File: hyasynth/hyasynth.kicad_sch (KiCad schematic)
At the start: 37 parts, among them J1 Conn_01x04_Male, J2 Conn_01x02_Male, J3 Conn_01x07_Male, J4 Conn_01x02_Male, J5 Conn_01x02_Male, SW1 Power Switch, SW10 G# Ab, SW11 A, SW12 A# Bb, SW13 B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

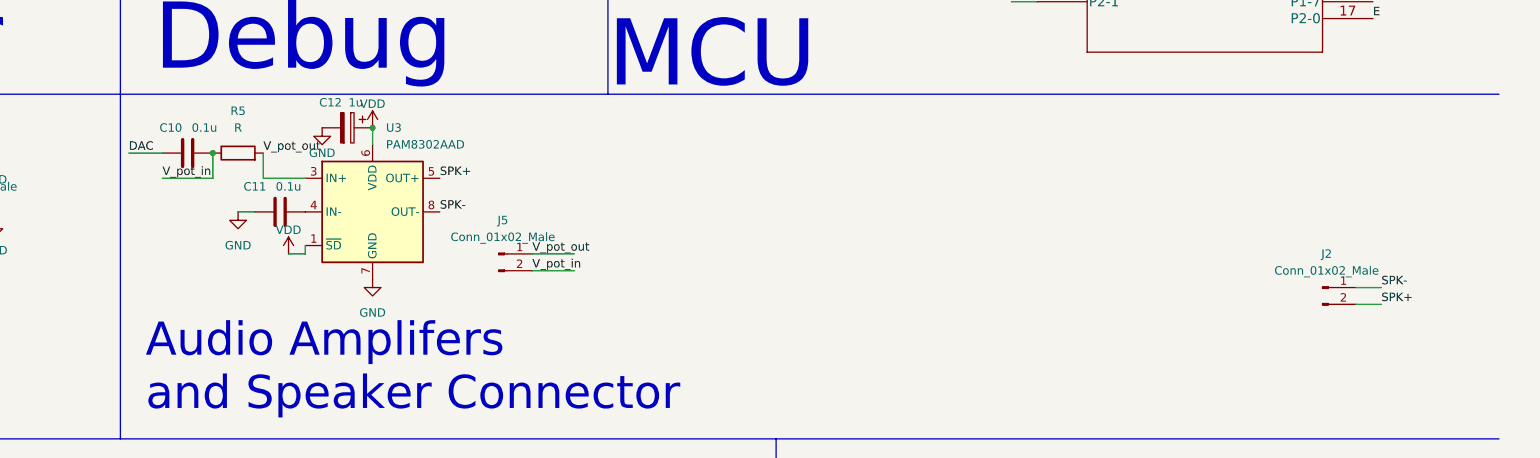
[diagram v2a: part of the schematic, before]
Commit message: borrowed new button footprint
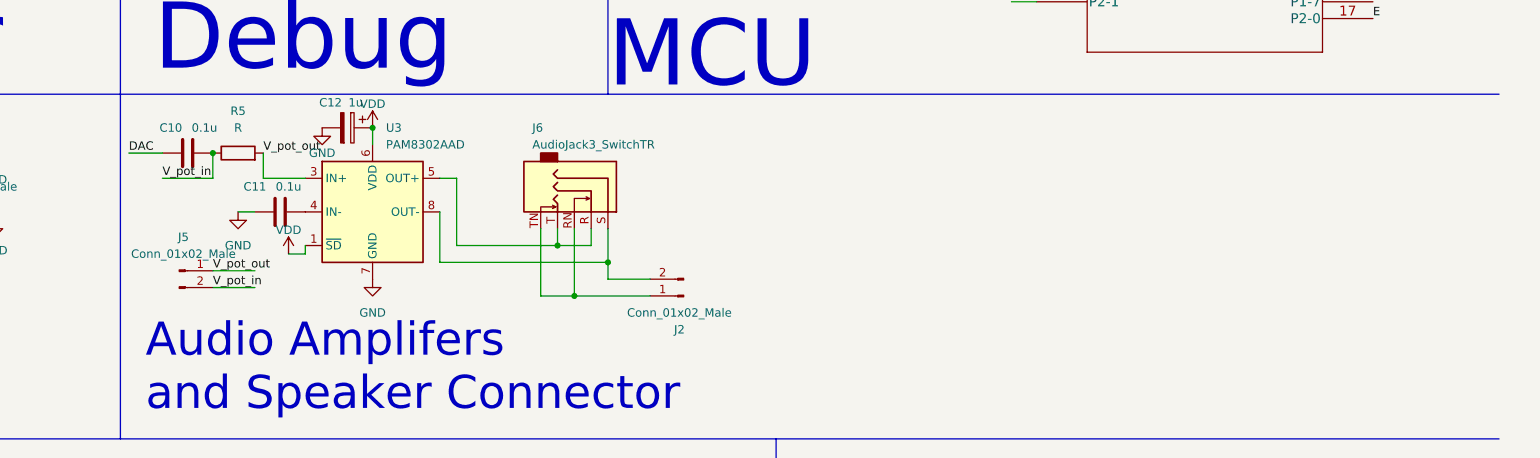
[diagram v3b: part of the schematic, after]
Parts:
- added J6: AudioJack3_SwitchTR, symbol Connector:AudioJack3_SwitchTR
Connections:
- net SPK+: no longer names the net of U3.5 (OUT+)
- net SPK+: now also J6.R, J6.T; no longer J2.2 (Pin_2)
- net SPK-: no longer names the net of J2.1 (Pin_1)
- net SPK-: now also J6.RN, J6.TN; no longer U3.8 (OUT-)
- new net: J2.2 (Pin_2), J6.S, U3.8 (OUT-)
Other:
- moved on the sheet: J2, J5
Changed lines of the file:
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@@
   (junction (at 101.6 175.26) (diameter 0) (color 0 0 0 0)
   )
+  (junction (at 151.13 109.22) (diameter 0) (color 0 0 0 0)
+  )
   (junction (at 158.75 40.64) (diameter 0) (color 0 0 0 0)
   )
   (junction (at 132.08 185.42) (diameter 0) (color 0 0 0 0)
   )
+  (junction (at 146.05 114.3) (diameter 0) (color 0 0 0 0)
+  )
   (junction (at 158.75 29.21) (diameter 0) (color 0 0 0 0)
   )
@@
   (junction (at 69.85 175.26) (diameter 0) (color 0 0 0 0)
   )
+  (junction (at 143.51 106.68) (diameter 0) (color 0 0 0 0)
+  )
   (junction (at 91.44 92.71) (diameter 0) (color 0 0 0 0)
   )
@@
     (stroke (width 0) (type default) (color 0 0 0 0))
   )
+  (wire (pts (xy 146.05 104.14) (xy 146.05 114.3))
+    (stroke (width 0) (type default) (color 0 0 0 0))
+  )
   (wire (pts (xy 119.38 36.83) (xy 123.19 36.83))
     (stroke (width 0) (type default) (color 0 0 0 0))
   )
+  (wire (pts (xy 140.97 104.14) (xy 140.97 114.3))
+    (stroke (width 0) (type default) (color 0 0 0 0))
+  )
   (wire (pts (xy 99.06 96.52) (xy 105.41 96.52))
     (stroke (width 0) (type default) (color 0 0 0 0))
@@
     (stroke (width 0) (type default) (color 0 0 0 0))
   )
-  (wire (pts (xy 264.16 113.03) (xy 267.97 113.03))
-    (stroke (width 0) (type default) (color 0 0 0 0))
-  )
   (wire (pts (xy 132.08 185.42) (xy 151.13 185.42))
     (stroke (width 0) (type default) (color 0 0 0 0))
@@
     (stroke (width 0) (type default) (color 0 0 0 0))
   )
+  (wire (pts (xy 143.51 106.68) (xy 148.59 106.68))
+    (stroke (width 0) (type default) (color 0 0 0 0))
+  )
   (polyline (pts (xy 77.47 83.82) (xy 77.47 135.89))
     (stroke (width 0) (type default) (color 0 0 0 0))
@@
     (stroke (width 0) (type default) (color 0 0 0 0))
   )
+  (wire (pts (xy 143.51 104.14) (xy 143.51 106.68))
+    (stroke (width 0) (type default) (color 0 0 0 0))
+  )
   (polyline (pts (xy 77.47 83.82) (xy 151.13 83.82))
     (stroke (width 0) (type default) (color 0 0 0 0))
@@
     (stroke (width 0) (type default) (color 0 0 0 0))
   )
-  (wire (pts (xy 139.7 110.49) (xy 146.05 110.49))
+  (wire (pts (xy 91.44 113.03) (xy 97.79 113.03))
     (stroke (width 0) (type default) (color 0 0 0 0))
   )
@@
     (stroke (width 0) (type default) (color 0 0 0 0))
   )
-  (wire (pts (xy 264.16 115.57) (xy 267.97 115.57))
-    (stroke (width 0) (type default) (color 0 0 0 0))
-  )
   (wire (pts (xy 158.75 40.64) (xy 170.18 40.64))
     (stroke (width 0) (type default) (color 0 0 0 0))
@@
     (stroke (width 0) (type default) (color 0 0 0 0))
   )
+  (wire (pts (xy 140.97 114.3) (xy 146.05 114.3))
+    (stroke (width 0) (type default) (color 0 0 0 0))
+  )
   (wire (pts (xy 212.09 31.75) (xy 215.9 31.75))
     (stroke (width 0) (type default) (color 0 0 0 0))
@@
     (stroke (width 0) (type default) (color 0 0 0 0))
   )
-  (wire (pts (xy 139.7 107.95) (xy 146.05 107.95))
+  (wire (pts (xy 125.73 101.6) (xy 125.73 109.22))
+    (stroke (width 0) (type default) (color 0 0 0 0))
+  )
+  (wire (pts (xy 151.13 111.76) (xy 151.13 109.22))
+    (stroke (width 0) (type default) (color 0 0 0 0))
+  )
+  (wire (pts (xy 91.44 110.49) (xy 97.79 110.49))
     (stroke (width 0) (type default) (color 0 0 0 0))
   )
@@
     (stroke (width 0) (type default) (color 0 0 0 0))
   )
+  (wire (pts (xy 125.73 96.52) (xy 128.27 96.52))
+    (stroke (width 0) (type default) (color 0 0 0 0))
+  )
   (polyline (pts (xy 176.53 135.89) (xy 285.75 135.89))
     (stroke (width 0) (type default) (color 0 0 0 0))
@@
     (stroke (width 0) (type default) (color 0 0 0 0))
   )
+  (wire (pts (xy 128.27 96.52) (xy 128.27 106.68))
+    (stroke (width 0) (type default) (color 0 0 0 0))
+  )
   (wire (pts (xy 86.36 185.42) (xy 101.6 185.42))
     (stroke (width 0) (type default) (color 0 0 0 0))
@@
     (stroke (width 0) (type default) (color 0 0 0 0))
   )
+  (wire (pts (xy 151.13 109.22) (xy 151.13 104.14))
+    (stroke (width 0) (type default) (color 0 0 0 0))
+  )
   (wire (pts (xy 252.73 158.75) (xy 267.97 158.75))
     (stroke (width 0) (type default) (color 0 0 0 0))
@@
     (stroke (width 0) (type default) (color 0 0 0 0))
   )
+  (wire (pts (xy 148.59 106.68) (xy 148.59 104.14))
+    (stroke (width 0) (type default) (color 0 0 0 0))
+  )
   (wire (pts (xy 44.45 167.64) (xy 38.1 167.64))
     (stroke (width 0) (type default) (color 0 0 0 0))
   )
+  (wire (pts (xy 157.48 111.76) (xy 151.13 111.76))
+    (stroke (width 0) (type default) (color 0 0 0 0))
+  )
   (wire (pts (xy 181.61 36.83) (xy 181.61 40.64))
     (stroke (width 0) (type default) (color 0 0 0 0))
@@
     (stroke (width 0) (type default) (color 0 0 0 0))
   )
+  (wire (pts (xy 125.73 109.22) (xy 151.13 109.22))
+    (stroke (width 0) (type default) (color 0 0 0 0))
+  )
   (wire (pts (xy 38.1 185.42) (xy 54.61 185.42))
     (stroke (width 0) (type default) (color 0 0 0 0))
   )
+  (wire (pts (xy 146.05 114.3) (xy 157.48 114.3))
+    (stroke (width 0) (type default) (color 0 0 0 0))
+  )
   (wire (pts (xy 191.77 34.29) (xy 191.77 29.21))
     (stroke (width 0) (type default) (color 0 0 0 0))
@@
   )
   (wire (pts (xy 266.7 31.75) (xy 276.86 31.75))
+    (stroke (width 0) (type default) (color 0 0 0 0))
+  )
+  (wire (pts (xy 128.27 106.68) (xy 143.51 106.68))
     (stroke (width 0) (type default) (color 0 0 0 0))
   )
@@
     (effects (font (size 1.27 1.27)) (justify left bottom))
   )
-  (label "SPK+" (at 267.97 115.57 0)
-    (effects (font (size 1.27 1.27)) (justify left bottom))
-  )
   (label "Uart_RX" (at 31.75 106.68 0)
     (effects (font (size 1.27 1.27)) (justify left bottom))
@@
     (effects (font (size 1.27 1.27)) (justify left bottom))
   )
-  (label "SPK+" (at 125.73 96.52 0)
-    (effects (font (size 1.27 1.27)) (justify left bottom))
-  )
   (label "Up" (at 212.09 57.15 0)
     (effects (font (size 1.27 1.27)) (justify left bottom))
@@
     (effects (font (size 1.27 1.27)) (justify left bottom))
   )
-  (label "SPK-" (at 125.73 101.6 0)
-    (effects (font (size 1.27 1.27)) (justify left bottom))
-  )
   (label "Low_C" (at 212.09 62.23 0)
     (effects (font (size 1.27 1.27)) (justify left bottom))
@@
     (effects (font (size 1.27 1.27)) (justify left bottom))
   )
-  (label "SPK-" (at 267.97 113.03 0)
-    (effects (font (size 1.27 1.27)) (justify left bottom))
-  )
   (label "Debug_Power" (at 48.26 33.02 0)
     (effects (font (size 1.27 1.27)) (justify left bottom))
@@
     (effects (font (size 1.27 1.27)) (justify left bottom))
   )
-  (label "V_pot_out" (at 139.7 107.95 0)
+  (label "V_pot_out" (at 91.44 110.49 0)
     (effects (font (size 1.27 1.27)) (justify left bottom))
   )
@@
     (effects (font (size 1.27 1.27)) (justify left bottom))
   )
-  (label "V_pot_in" (at 139.7 110.49 0)
+  (label "V_pot_in" (at 91.44 113.03 0)
     (effects (font (size 1.27 1.27)) (justify left bottom))
   )
@@
     )
     (pin "1")
+  )
+  (symbol (lib_id "Connector:AudioJack3_SwitchTR") (at 148.59 99.06 270) (unit 1)
+    (in_bom yes) (on_board yes)
+    (property "Reference" "J6" (id 0) (at 139.7 88.9 90)
+      (effects (font (size 1.27 1.27)) (justify left))
+    )
+    (property "Value" "AudioJack3_SwitchTR" (id 1) (at 139.7 91.44 90)
+      (effects (font (size 1.27 1.27)) (justify left))
+    )
+    (property "Footprint" "" (id 2) (at 148.59 99.06 0)
+      (effects (font (size 1.27 1.27)) hide)
+    )
+    (property "Datasheet" "~" (id 3) (at 148.59 99.06 0)
+      (effects (font (size 1.27 1.27)) hide)
+    )
+    (pin "R")
+    (pin "RN")
+    (pin "S")
+    (pin "T")
+    (pin "TN")
   )
   (symbol (lib_id "Switch:SW_Push") (at 257.81 152.4 0) (unit 1)
@@
     (pin "2")
   )
-  (symbol (lib_id "Connector:Conn_01x02_Male") (at 134.62 107.95 0) (unit 1)
-    (in_bom yes) (on_board yes) (fields_autoplaced)
-    (property "Reference" "J5" (id 0) (at 135.255 102.87 0))
-    (property "Value" "Conn_01x02_Male" (id 1) (at 135.255 105.41 0))
-    (property "Footprint" "Connector_PinHeader_2.54mm:PinHeader_1x02_P2.54mm_Vertical" (id 2) (at 134.62 107.95 0)
-      (effects (font (size 1.27 1.27)) hide)
-    )
-    (property "Datasheet" "~" (id 3) (at 134.62 107.95 0)
+  (symbol (lib_id "Connector:Conn_01x02_Male") (at 86.36 110.49 0) (unit 1)
+    (in_bom yes) (on_board yes) (fields_autoplaced)
+    (property "Reference" "J5" (id 0) (at 86.995 105.41 0))
+    (property "Value" "Conn_01x02_Male" (id 1) (at 86.995 107.95 0))
+    (property "Footprint" "Connector_PinHeader_2.54mm:PinHeader_1x02_P2.54mm_Vertical" (id 2) (at 86.36 110.49 0)
+      (effects (font (size 1.27 1.27)) hide)
+    )
+    (property "Datasheet" "~" (id 3) (at 86.36 110.49 0)
       (effects (font (size 1.27 1.27)) hide)
     )
@@
     (pin "4")
   )
-  (symbol (lib_id "Connector:Conn_01x02_Male") (at 259.08 113.03 0) (unit 1)
+  (symbol (lib_id "Connector:Conn_01x02_Male") (at 162.56 114.3 180) (unit 1)
     (in_bom yes) (on_board yes)
-    (property "Reference" "J2" (id 0) (at 259.715 107.95 0))
-    (property "Value" "Conn_01x02_Male" (id 1) (at 259.715 110.49 0))
-    (property "Footprint" "Connector_PinHeader_2.54mm:PinHeader_1x02_P2.54mm_Vertical" (id 2) (at 259.08 113.03 0)
-      (effects (font (size 1.27 1.27)) hide)
-    )
-    (property "Datasheet" "~" (id 3) (at 259.08 113.03 0)
+    (property "Reference" "J2" (id 0) (at 161.925 119.38 0))
+    (property "Value" "Conn_01x02_Male" (id 1) (at 161.925 116.84 0))
+    (property "Footprint" "Connector_PinHeader_2.54mm:PinHeader_1x02_P2.54mm_Vertical" (id 2) (at 162.56 114.3 0)
+      (effects (font (size 1.27 1.27)) hide)
+    )
+    (property "Datasheet" "~" (id 3) (at 162.56 114.3 0)
       (effects (font (size 1.27 1.27)) hide)
     )
@@
       (reference "J5") (unit 1) (value "Conn_01x02_Male") (footprint "Connector_PinHeader_2.54mm:PinHeader_1x02_P2.54mm_Vertical")
     )
+    (path "/302f71e7-221e-4108-92c1-cb6009e0ebe5"
+      (reference "J6") (unit 1) (value "AudioJack3_SwitchTR") (footprint "")
+    )
     (path "/e38ef933-cad1-4eee-acc2-e0e397c973b5"

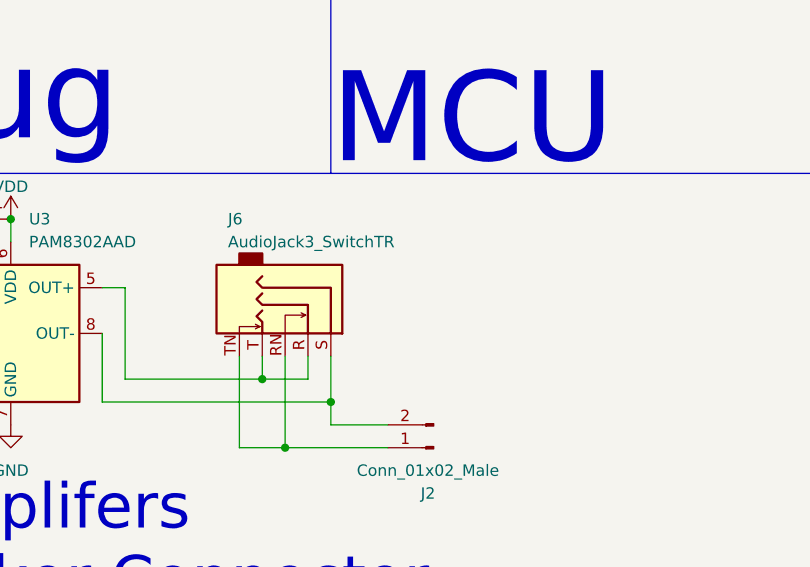
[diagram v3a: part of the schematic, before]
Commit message: Added jack and switch and repositioned components
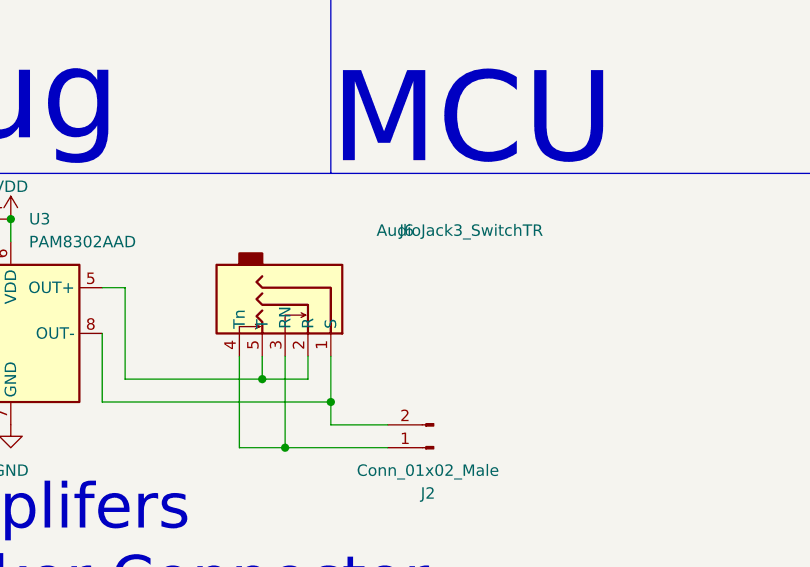
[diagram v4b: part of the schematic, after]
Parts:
- J6: footprint (none) -> Jack:Jack
- SW1: footprint Connector_PinHeader_2.54mm:PinHeader_1x03_P2.54mm_Vertical -> Switch:Slide Switch
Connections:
- net at J2.2 (Pin_2), U3.8 (OUT-): now also J6.1 (S); no longer J6.S
- new net: J6.2 (R), J6.5 (T), U3.5 (OUT+)
- new net: J2.1 (Pin_1), J6.3 (RN), J6.4 (Tn)
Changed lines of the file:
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@@
   (symbol (lib_id "Connector:AudioJack3_SwitchTR") (at 148.59 99.06 270) (unit 1)
     (in_bom yes) (on_board yes)
-    (property "Reference" "J6" (id 0) (at 139.7 88.9 90)
-      (effects (font (size 1.27 1.27)) (justify left))
-    )
-    (property "Value" "AudioJack3_SwitchTR" (id 1) (at 139.7 91.44 90)
-      (effects (font (size 1.27 1.27)) (justify left))
-    )
-    (property "Footprint" "" (id 2) (at 148.59 99.06 0)
+    (property "Reference" "J6" (id 0) (at 158.75 90.17 90)
+      (effects (font (size 1.27 1.27)) (justify left))
+    )
+    (property "Value" "AudioJack3_SwitchTR" (id 1) (at 156.21 90.17 90)
+      (effects (font (size 1.27 1.27)) (justify left))
+    )
+    (property "Footprint" "Jack:Jack" (id 2) (at 153.67 96.52 0)
       (effects (font (size 1.27 1.27)) hide)
     )
@@
       (effects (font (size 1.27 1.27)) hide)
     )
-    (pin "R")
-    (pin "RN")
-    (pin "S")
-    (pin "T")
-    (pin "TN")
+    (pin "2")
+    (pin "3")
+    (pin "1")
+    (pin "5")
+    (pin "4")
   )
   (symbol (lib_id "Switch:SW_Push") (at 257.81 152.4 0) (unit 1)
@@
     (property "Reference" "SW1" (id 0) (at 46.99 24.13 90))
     (property "Value" "Power Switch" (id 1) (at 52.07 26.67 90))
-    (property "Footprint" "Connector_PinHeader_2.54mm:PinHeader_1x03_P2.54mm_Vertical" (id 2) (at 41.91 26.67 0)
+    (property "Footprint" "Switch:Slide Switch" (id 2) (at 41.91 26.67 0)
       (effects (font (size 1.27 1.27)) hide)
     )
@@
     )
     (path "/302f71e7-221e-4108-92c1-cb6009e0ebe5"
-      (reference "J6") (unit 1) (value "AudioJack3_SwitchTR") (footprint "")
+      (reference "J6") (unit 1) (value "AudioJack3_SwitchTR") (footprint "Jack:Jack")
     )
     (path "/e38ef933-cad1-4eee-acc2-e0e397c973b5"
@@
     )
     (path "/8edc3100-86dd-4549-b6e6-d3e637e4160d"
-      (reference "SW1") (unit 1) (value "Power Switch") (footprint "Connector_PinHeader_2.54mm:PinHeader_1x03_P2.54mm_Vertical")
+      (reference "SW1") (unit 1) (value "Power Switch") (footprint "Switch:Slide Switch")
     )
     (path "/7e72304a-4161-4a22-8d65-75ee76dcdf69"
